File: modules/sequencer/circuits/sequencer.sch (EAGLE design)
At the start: 50 parts, among them IC1 LM555N, IC2 LM324N

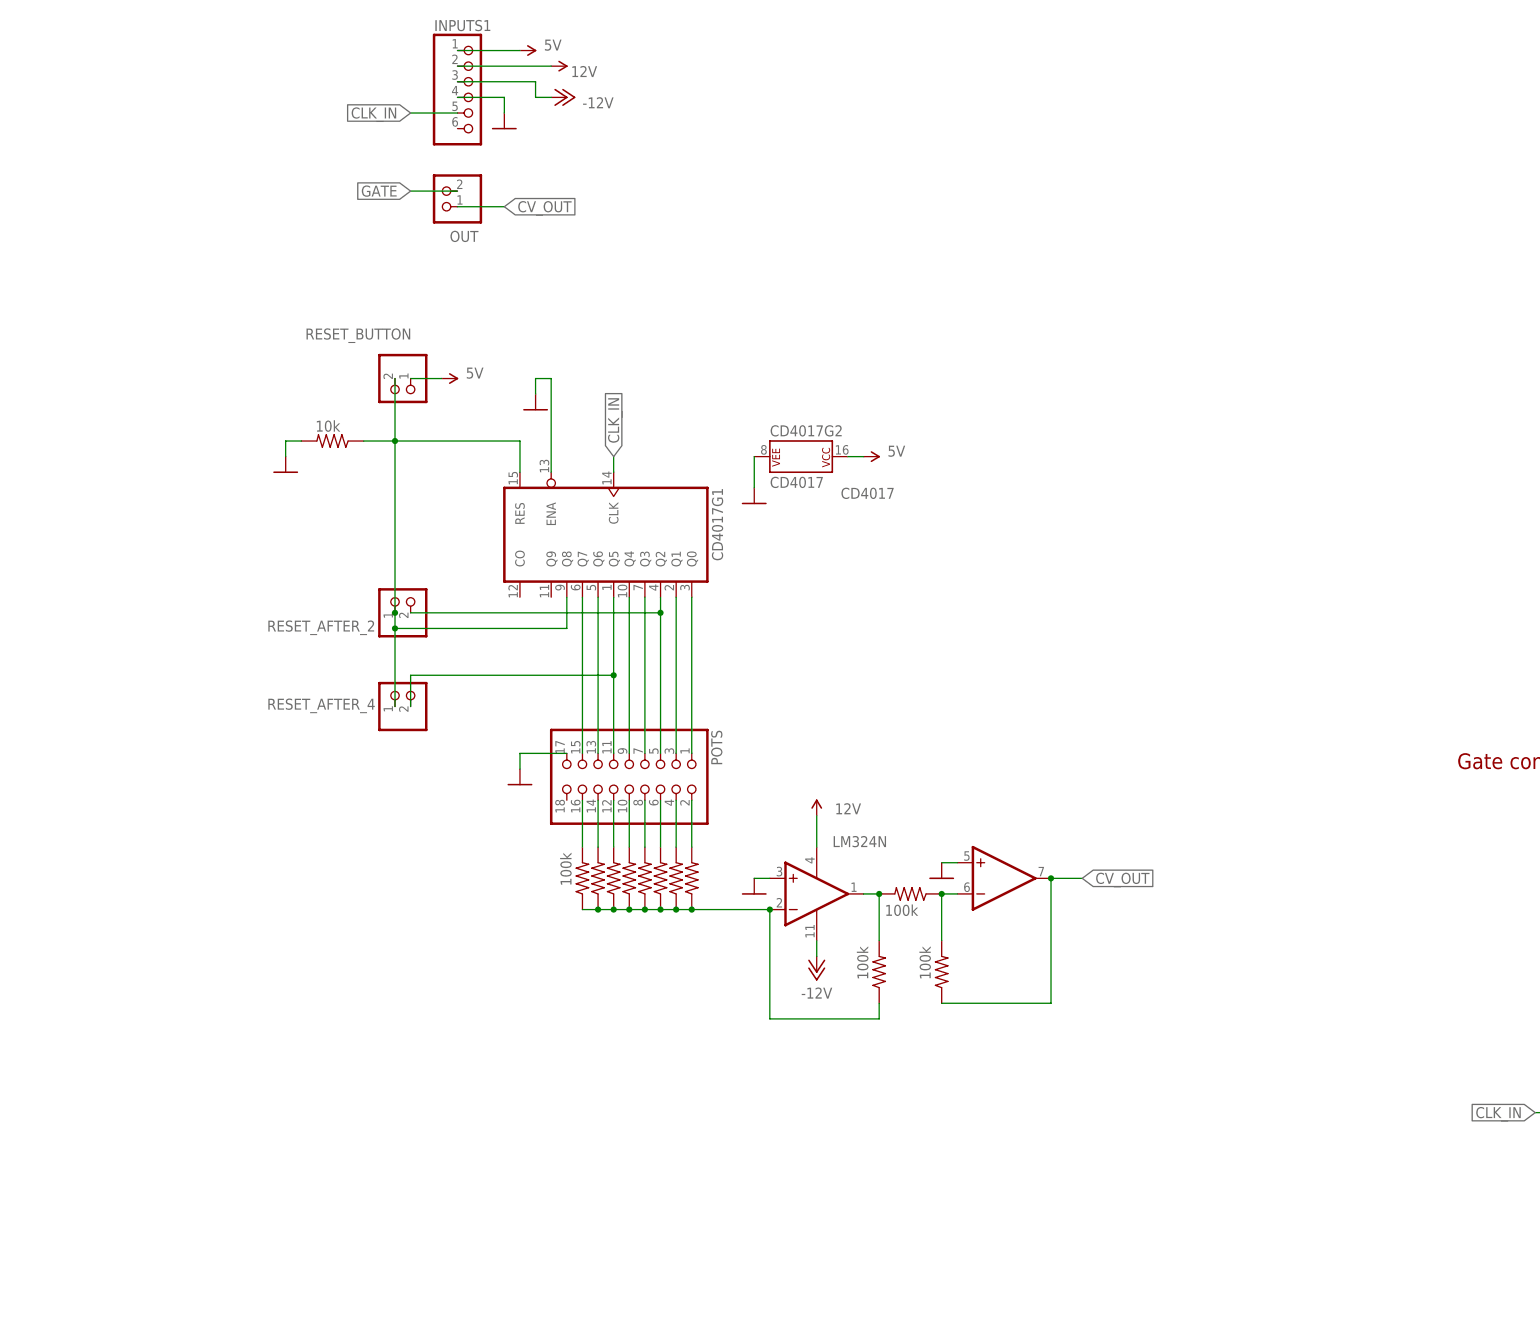
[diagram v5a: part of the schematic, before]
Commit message: Adding counter to seq
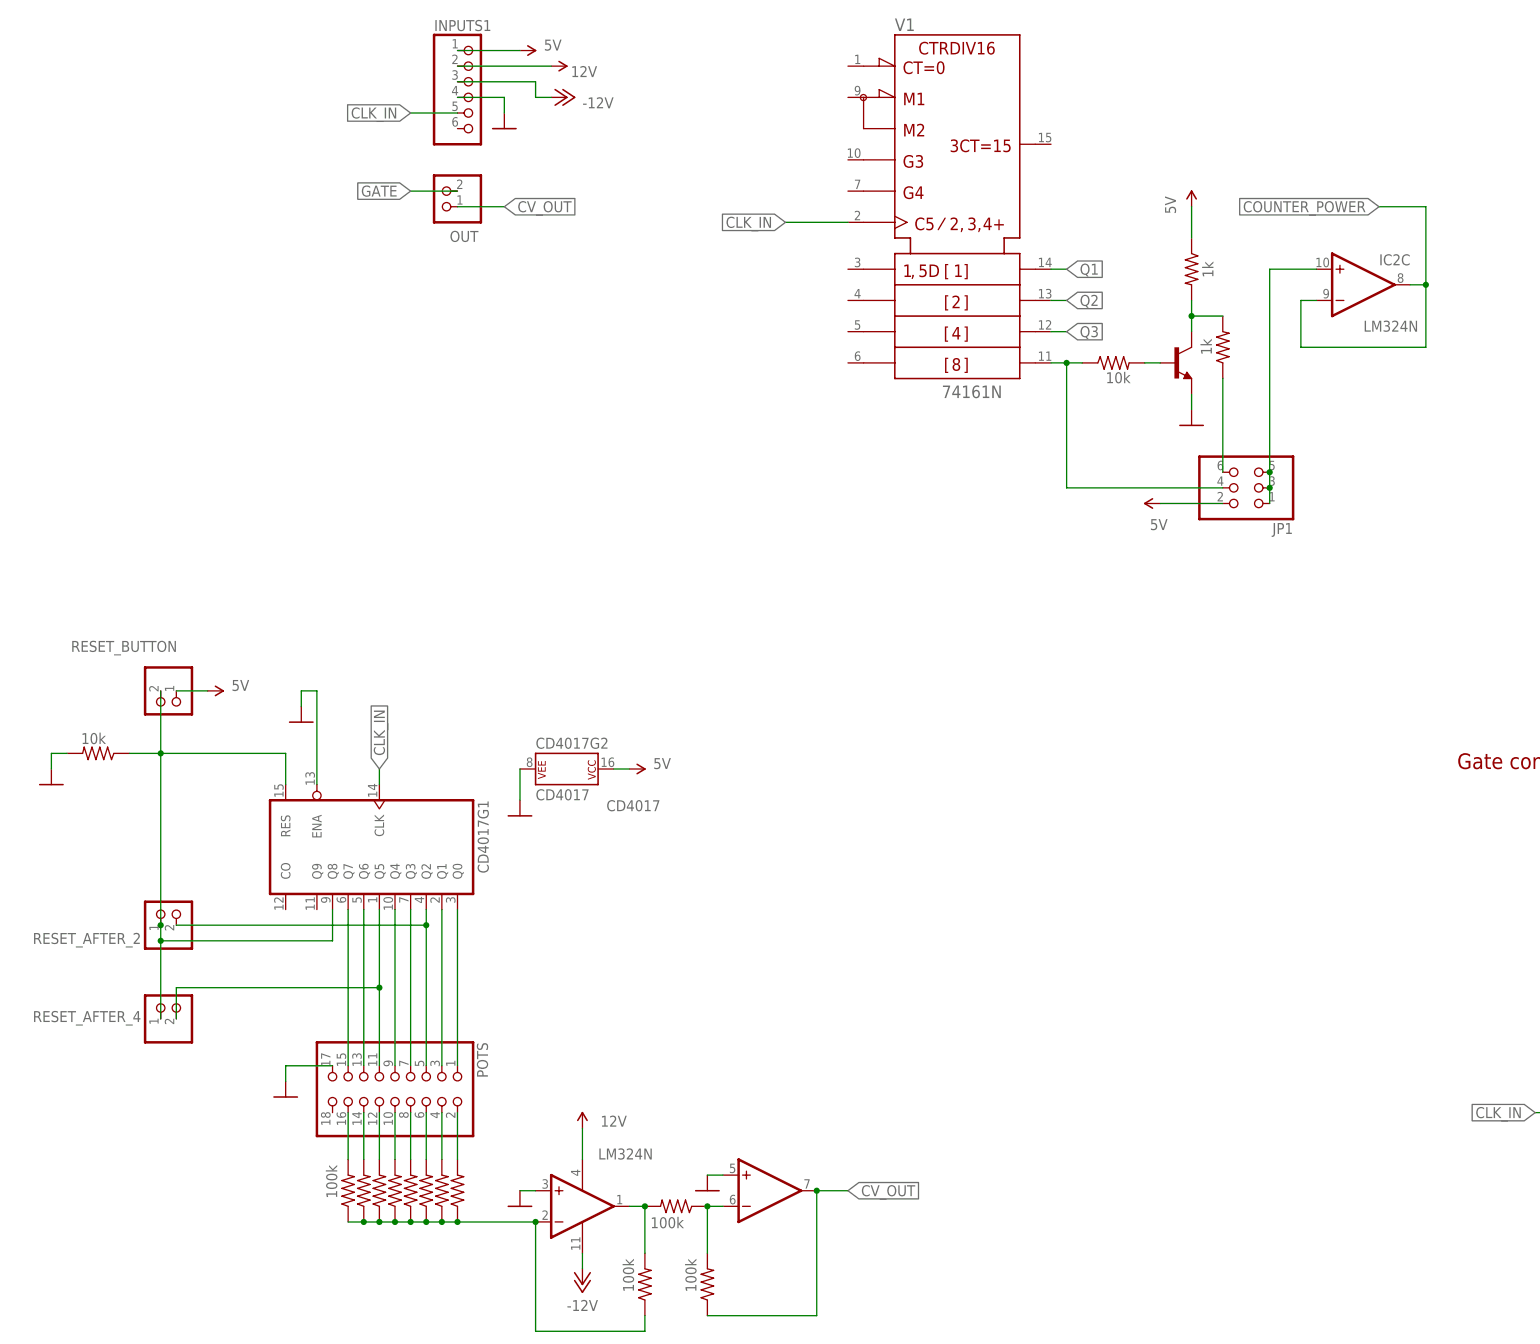
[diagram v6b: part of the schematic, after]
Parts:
- added 1K2, 1K6: 1k, adafruit:R-US_0207/12
- added 1K5: 10k, adafruit:R-US_0207/12
- added 2N3: (no value), transistor-neu-to92:2N4401-NPN-TO92-EBC
- added JP1: (no value), pinhead:PINHD-2X3
- added V1: 74161N, 74ttl-din:74161N
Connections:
- new net COUNTER_POWER: IC2C.-IN, IC2C.OUT
- new net N$37: 1K5.2, 2N3.B
- new net N$38: 1K5.1, JP1.4, V11.QD
- new net N$39: 1K2.2, 1K6.2, 2N3.C
- new net N$40: 1K2.1, JP1.6
- new net N$42: IC2C.+IN, JP1.1, JP1.3, JP1.5
- new net Q1: V11.QA
- new net Q2: V11.QB
- new net Q3: V11.QC
- net 5V: now also 1K6.1, JP1.2
- net CLK_IN: now also V11.CLK
- net GND: now also 2N3.E
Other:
- moved on the sheet: CD4017G1, CD4017G2, POTS, RESET_AFTER_2, RESET_AFTER_4, RESET_BUTTON

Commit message: midi2cv
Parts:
- removed 1K2, 1K6: 1k, adafruit:R-US_0207/12
- removed 1K5: 10k, adafruit:R-US_0207/12
- removed 2N3: (no value), transistor-neu-to92:2N4401-NPN-TO92-EBC
- removed JP1: (no value), pinhead:PINHD-2X3
- added IC3: 4056N, 40xx:4056N
- added R24: 10k, adafruit:R-US_0207/12
- C2: value 220uf -> 100uf
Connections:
- removed net COUNTER_POWER: IC2C.-IN, IC2C.OUT
- removed net N$37: 1K5.2, 2N3.B
- removed net N$38: 1K5.1, JP1.4, V11.QD
- removed net N$39: 1K2.2, 1K6.2, 2N3.C
- removed net N$40: 1K2.1, JP1.6
- removed net N$42: IC2C.+IN, JP1.1, JP1.3, JP1.5
- net 5V: now also V11.!CLR, V11.!LOAD, V11.ENP, V11.ENT; no longer 1K6.1, JP1.2
- net CLK_IN: now also R24.1
- net GND: now also IC3A.I3, R24.2; no longer 2N3.E

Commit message: sequencer board
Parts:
- removed LED1, LED2, LED3, LED4, LED5, LED6, LED7, LED8: (no value), adafruit:LED5MM
- removed R19: 330, adafruit:R-US_0207/12
- added D2: 157119S12801, Wurth_7 Segments Display_WL-T7DS:WL-T7DS_0.39INCH_COMMON-ANODE_157119S12801
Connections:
- new net N$37: IC3A.A, R1.1
- new net N$38: IC3A.B, R13.1
- new net N$39: IC3A.C, R14.1
- new net N$40: IC3A.D, R15.1
- new net N$41: IC3A.E, R16.1
- new net N$42: IC3A.G, R18.1
- net 5V: now also D2.+, IC3A.DFI, IC3A.ST, IC3P.VCC, V1/+UB.+UB
- net GND: now also IC3P.GND, IC3P.VEE, V1/-UB.-UB; no longer LED1.C, LED2.C, LED3.C, LED4.C, LED5.C, LED6.C, LED7.C, LED8.C
- net N$22: now also IC3A.F, R17.1; no longer LED3.A, R14.1
- net N$23: now also D2.10, R18.2; no longer LED4.A, R15.1
- net N$24: now also D2.9, R17.2; no longer LED5.A, R16.1
- net N$25: now also D2.1, R16.2; no longer LED6.A, R17.1
- net N$26: now also D2.2, R15.2; no longer LED7.A, R18.1
- net N$27: now also D2.4, R14.2; no longer LED8.A, R19.1
- net N$28: now also D2.6, R13.2; no longer LED2.A, R13.1
- net N$29: now also D2.7, R1.2; no longer LED1.A, R1.1
- net Q1: now also IC3A.I0
- net Q2: now also IC3A.I1
- net Q3: now also IC3A.I2
